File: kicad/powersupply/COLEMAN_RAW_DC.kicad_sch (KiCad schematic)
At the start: 8 parts

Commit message: up
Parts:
- C15, C16: footprint (none) -> Capacitor_THT:CP_Radial_D25.0mm_P10.00mm_SnapIn; MPN (none) -> SLPX153M025C7P3
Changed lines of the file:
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@@
-    )
-  )
-  (symbol (lib_id "Device:C_Polarized") (at 127 74.93 0) (unit 1)
-    (in_bom yes) (on_board yes) (dnp no)
-    (property "Reference" "C16" (at 128.27 72.39 0)
-      (effects (font (size 1.27 1.27)) (justify left))
-    )
-    (property "Value" "15000u 25 V" (at 119.38 77.47 0)
-      (effects (font (size 1.27 1.27)) (justify left))
-    )
-    (property "Footprint" "" (at 127.9652 78.74 0)
-      (effects (font (size 1.27 1.27)) hide)
-    )
-    (property "Datasheet" "" (at 127 74.93 0)
-      (effects (font (size 1.27 1.27)) hide)
-    )
-    (property "MPN" "" (at 127 74.93 0)
-      (effects (font (size 1.27 1.27)) hide)
-    )
-    (pin "1")
-    (pin "2")
-    (instances
-      (project "OSDEHA_PSU"
-        (path "/ca37e2fa-48ac-4eb3-a7a4-1e3bbee61661/727c75f6-edc2-4fc0-8e3e-14cbc2040e98"
-          (reference "C16") (unit 1)
-        )
-        (path "/ca37e2fa-48ac-4eb3-a7a4-1e3bbee61661/5494a183-e083-4795-ba51-682672d147b4"
-          (reference "C18") (unit 1)
-        )
-      )
     )
   )
@@
       (effects (font (size 1.27 1.27)) (justify left))
     )
-    (property "Footprint" "" (at 110.1852 78.74 0)
+    (property "Footprint" "Capacitor_THT:CP_Radial_D25.0mm_P10.00mm_SnapIn" (at 110.1852 78.74 0)
       (effects (font (size 1.27 1.27)) hide)
     )
-    (property "Datasheet" "" (at 109.22 74.93 0)
+    (property "Datasheet" "https://www.cde.com/resources/catalogs/SLPX.pdf" (at 109.22 74.93 0)
       (effects (font (size 1.27 1.27)) hide)
     )
-    (property "MPN" "" (at 109.22 74.93 0)
+    (property "MPN" "SLPX153M025C7P3 " (at 109.22 74.93 0)
       (effects (font (size 1.27 1.27)) hide)
     )
@@
         )
       )
+    )
+  )
+  (symbol (lib_id "Device:C_Polarized") (at 127 74.93 0) (unit 1)
+    (in_bom yes) (on_board yes) (dnp no)
+    (property "Reference" "C16" (at 128.27 72.39 0)
+      (effects (font (size 1.27 1.27)) (justify left))
+    )
+    (property "Value" "15000u 25 V" (at 119.38 77.47 0)
+      (effects (font (size 1.27 1.27)) (justify left))
+    )
+    (property "Footprint" "Capacitor_THT:CP_Radial_D25.0mm_P10.00mm_SnapIn" (at 127.9652 78.74 0)
+      (effects (font (size 1.27 1.27)) hide)
+    )
+    (property "Datasheet" "https://www.cde.com/resources/catalogs/SLPX.pdf" (at 127 74.93 0)
+      (effects (font (size 1.27 1.27)) hide)
+    )
+    (property "MPN" "SLPX153M025C7P3 " (at 127 74.93 0)
+      (effects (font (size 1.27 1.27)) hide)
+    )
+    (pin "1")
+    (pin "2")
+    (instances
+      (project "OSDEHA_PSU"
+        (path "/ca37e2fa-48ac-4eb3-a7a4-1e3bbee61661/727c75f6-edc2-4fc0-8e3e-14cbc2040e98"
+          (reference "C16") (unit 1)
+        )
+        (path "/ca37e2fa-48ac-4eb3-a7a4-1e3bbee61661/5494a183-e083-4795-ba51-682672d147b4"
+          (reference "C18") (unit 1)
+        )
+      )

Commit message: up
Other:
- note added: "Raw DC supply for Coleman DHT filament regulator"
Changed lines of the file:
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@@
     (stroke (width 0) (type default))
+  )
+  (text "Raw DC supply for Coleman DHT filament regulator" (at 72.39 53.34 0)
+    (effects (font (size 2 2) (thickness 0.508) bold) (justify left bottom))
   )
   (hierarchical_label "RAWDC+" (shape passive) (at 140.97 62.23 0) (fields_autoplaced)

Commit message: psu work
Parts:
- R39, R40: value 0.2 3 W -> 0.22 3 W; footprint (none) -> Resistor_THT:R_Axial_DIN0614_L14.3mm_D5.7mm_P15.24mm_Horizontal; MPN (none) -> CPF3R22000GNB14
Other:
- note added: "Raw DC supply for Coleman DHT filament regulator (floating!)"
- note removed: "Raw DC supply for Coleman DHT filament regulator"
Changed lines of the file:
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@@
     (stroke (width 0) (type default))
   )
-  (text "Raw DC supply for Coleman DHT filament regulator" (at 72.39 53.34 0)
+  (text "Raw DC supply for Coleman DHT filament regulator (floating!)"
+    (at 72.39 53.34 0)
     (effects (font (size 2 2) (thickness 0.508) bold) (justify left bottom))
   )
@@
       (effects (font (size 1.27 1.27)))
     )
-    (property "Value" "0.2 3 W" (at 118.11 90.17 90)
-      (effects (font (size 1.27 1.27)))
-    )
-    (property "Footprint" "" (at 118.11 89.408 90)
-      (effects (font (size 1.27 1.27)) hide)
-    )
-    (property "Datasheet" "" (at 118.11 87.63 0)
+    (property "Value" "0.22 3 W" (at 118.11 90.17 90)
+      (effects (font (size 1.27 1.27)))
+    )
+    (property "Footprint" "Resistor_THT:R_Axial_DIN0614_L14.3mm_D5.7mm_P15.24mm_Horizontal" (at 118.11 89.408 90)
+      (effects (font (size 1.27 1.27)) hide)
+    )
+    (property "Datasheet" "https://www.vishay.com/doc?31021" (at 118.11 87.63 0)
+      (effects (font (size 1.27 1.27)) hide)
+    )
+    (property "MPN" "CPF3R22000GNB14 " (at 118.11 87.63 90)
       (effects (font (size 1.27 1.27)) hide)
     )
@@
       (effects (font (size 1.27 1.27)))
     )
-    (property "Value" "0.2 3 W" (at 118.11 64.77 90)
-      (effects (font (size 1.27 1.27)))
-    )
-    (property "Footprint" "" (at 118.11 64.008 90)
-      (effects (font (size 1.27 1.27)) hide)
-    )
-    (property "Datasheet" "" (at 118.11 62.23 0)
-      (effects (font (size 1.27 1.27)) hide)
-    )
+    (property "Value" "0.22 3 W" (at 118.11 64.77 90)
+      (effects (font (size 1.27 1.27)))
+    )
+    (property "Footprint" "Resistor_THT:R_Axial_DIN0614_L14.3mm_D5.7mm_P15.24mm_Horizontal" (at 118.11 64.008 90)
+      (effects (font (size 1.27 1.27)) hide)
+    )
+    (property "Datasheet" "https://www.vishay.com/doc?31021" (at 118.11 62.23 0)
+      (effects (font (size 1.27 1.27)) hide)
+    )
+    (property "MPN" "CPF3R22000GNB14 " (at 118.11 62.23 90)
+      (effects (font (size 1.27 1.27)) hide)
+    )

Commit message: bleeders
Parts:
- added R44: 10k, Resistor_THT:R_Axial_DIN0207_L6.3mm_D2.5mm_P10.16mm_Horizontal, symbol Device:R
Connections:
- net at C15.2, D40.2 (A), D42.2 (A)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: now also R44.2
- net at C15.1, D39.1 (K), D41.1 (K)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: now also R44.1
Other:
- moved on the sheet: C15, C16, R39, R40

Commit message: MPNs and datasheet links
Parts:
- D39, D40, D41, D42: MPN (none) -> 1N5822
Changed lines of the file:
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@@
+      (effects (font (size 1.27 1.27)) hide)
+    )
+    (property "MPN" "1N5822" (at 91.44 82.55 90)
       (effects (font (size 1.27 1.27)) hide)
     )
@@
     )
     (property "Datasheet" "http://www.vishay.com/docs/88526/1n5820.pdf" (at 76.2 82.55 0)
+      (effects (font (size 1.27 1.27)) hide)
+    )
+    (property "MPN" "1N5822" (at 76.2 82.55 90)
       (effects (font (size 1.27 1.27)) hide)
     )
@@
       (effects (font (size 1.27 1.27)) hide)
     )
+    (property "MPN" "1N5822" (at 91.44 67.31 90)
+      (effects (font (size 1.27 1.27)) hide)
+    )
     (pin "2")
     (pin "1")
@@
       (effects (font (size 1.27 1.27)) hide)
     )
+    (property "MPN" "1N5822" (at 76.2 67.31 90)
+      (effects (font (size 1.27 1.27)) hide)
+    )

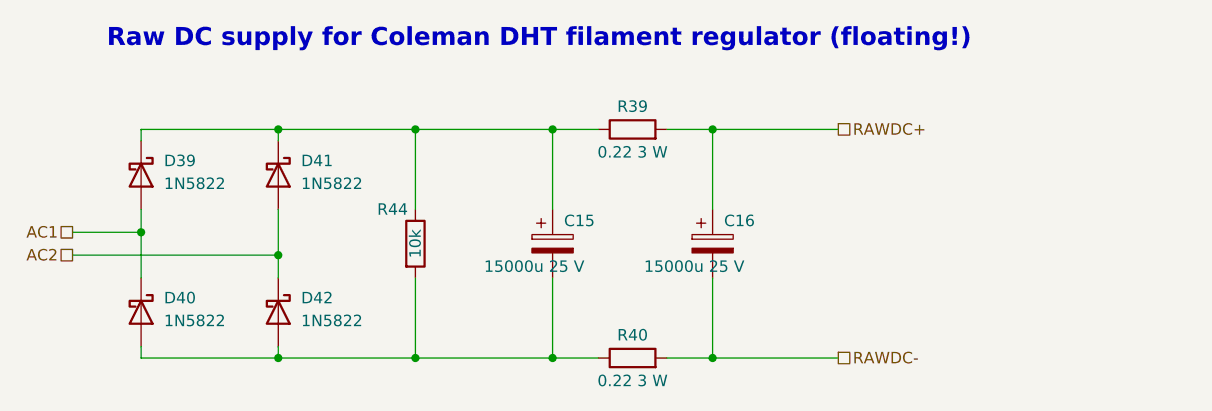
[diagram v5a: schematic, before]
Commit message: psu (del buffer, change output pass part)
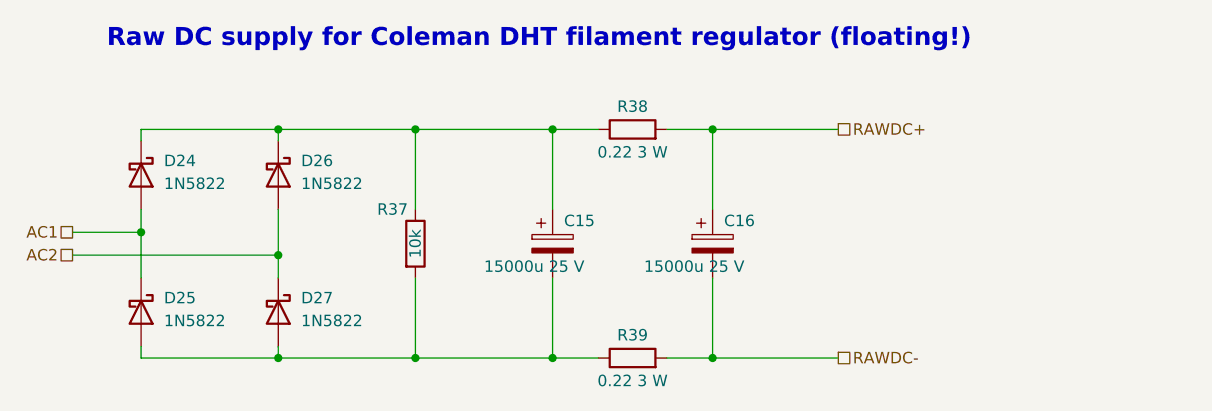
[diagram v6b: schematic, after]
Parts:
- renumbered D39 to D24, D40 to D25, D41 to D26, D42 to D27, R44 to R37, R39 to R38, R40 to R39

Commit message: psu
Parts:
- renumbered R37 to R34, R38 to R35, R39 to R36
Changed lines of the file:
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@@
   (symbol (lib_id "Device:R") (at 130.81 87.63 90) (unit 1)
     (in_bom yes) (on_board yes) (dnp no)
-    (property "Reference" "R39" (at 130.81 85.09 90)
+    (property "Reference" "R36" (at 130.81 85.09 90)
       (effects (font (size 1.27 1.27)))
     )
@@
       (project "OSDEHA_PSU"
         (path "/ca37e2fa-48ac-4eb3-a7a4-1e3bbee61661/727c75f6-edc2-4fc0-8e3e-14cbc2040e98"
+          (reference "R36") (unit 1)
+        )
+        (path "/ca37e2fa-48ac-4eb3-a7a4-1e3bbee61661/5494a183-e083-4795-ba51-682672d147b4"
           (reference "R39") (unit 1)
-        )
-        (path "/ca37e2fa-48ac-4eb3-a7a4-1e3bbee61661/5494a183-e083-4795-ba51-682672d147b4"
-          (reference "R42") (unit 1)
         )
       )
@@
   (symbol (lib_id "Device:R") (at 106.68 74.93 0) (unit 1)
     (in_bom yes) (on_board yes) (dnp no)
-    (property "Reference" "R37" (at 104.14 71.12 0)
+    (property "Reference" "R34" (at 104.14 71.12 0)
       (effects (font (size 1.27 1.27)))
     )
@@
       (project "OSDEHA_PSU"
         (path "/ca37e2fa-48ac-4eb3-a7a4-1e3bbee61661/727c75f6-edc2-4fc0-8e3e-14cbc2040e98"
+          (reference "R34") (unit 1)
+        )
+        (path "/ca37e2fa-48ac-4eb3-a7a4-1e3bbee61661/5494a183-e083-4795-ba51-682672d147b4"
           (reference "R37") (unit 1)
         )
-        (path "/ca37e2fa-48ac-4eb3-a7a4-1e3bbee61661/5494a183-e083-4795-ba51-682672d147b4"
-          (reference "R40") (unit 1)
-        )
       )
     )
@@
   (symbol (lib_id "Device:R") (at 130.81 62.23 90) (unit 1)
     (in_bom yes) (on_board yes) (dnp no)
-    (property "Reference" "R38" (at 130.81 59.69 90)
+    (property "Reference" "R35" (at 130.81 59.69 90)
       (effects (font (size 1.27 1.27)))
     )
@@
       (project "OSDEHA_PSU"
         (path "/ca37e2fa-48ac-4eb3-a7a4-1e3bbee61661/727c75f6-edc2-4fc0-8e3e-14cbc2040e98"
+          (reference "R35") (unit 1)
+        )
+        (path "/ca37e2fa-48ac-4eb3-a7a4-1e3bbee61661/5494a183-e083-4795-ba51-682672d147b4"
           (reference "R38") (unit 1)
         )
-        (path "/ca37e2fa-48ac-4eb3-a7a4-1e3bbee61661/5494a183-e083-4795-ba51-682672d147b4"
-          (reference "R41") (unit 1)
-        )
-      )
+      )
